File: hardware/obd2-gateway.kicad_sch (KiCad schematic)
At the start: 7 parts, among them J1 OBD-II 커넥터, U1 LM2596 (5.0V 조정), U2 SN65HVD230 (R2 제거!), U3 ESP32-S3 개발보드

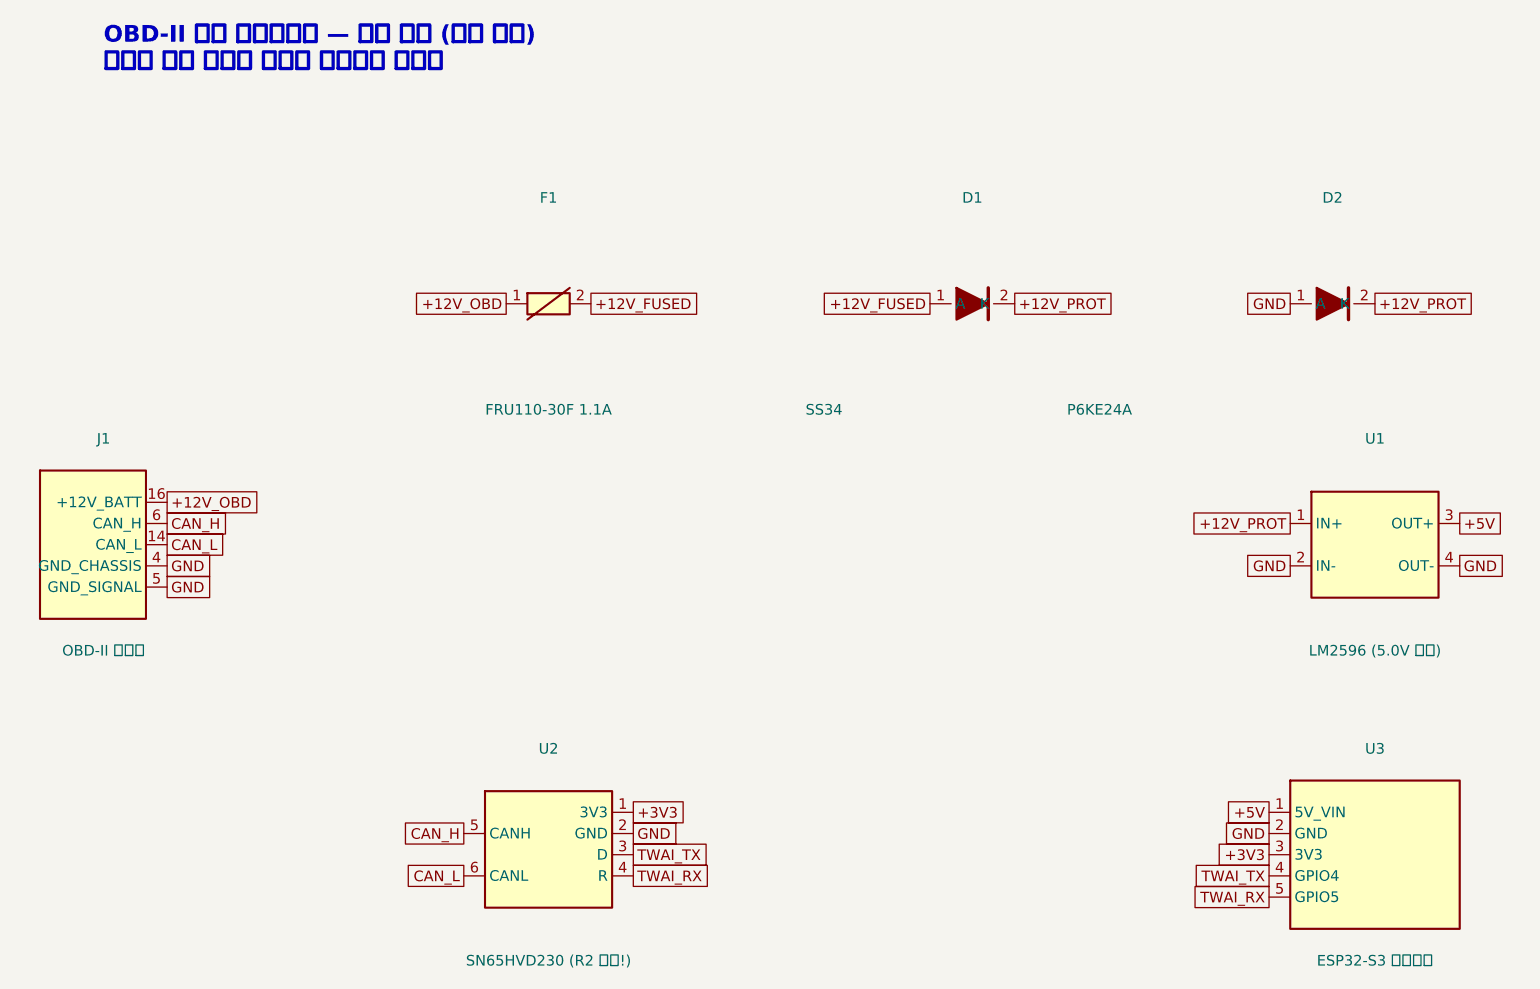
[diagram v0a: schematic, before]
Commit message: hardware: 회로도를 배선(wire) 방식으로 재작성 (Rev B, 초보자 가독성)
Co-Authored-By: Claude Fable 5 <noreply@anthropic.com>
Claude-Session: https://claude.ai/code/session_015Lj2iN8K2AKiUuQKmtXaeP
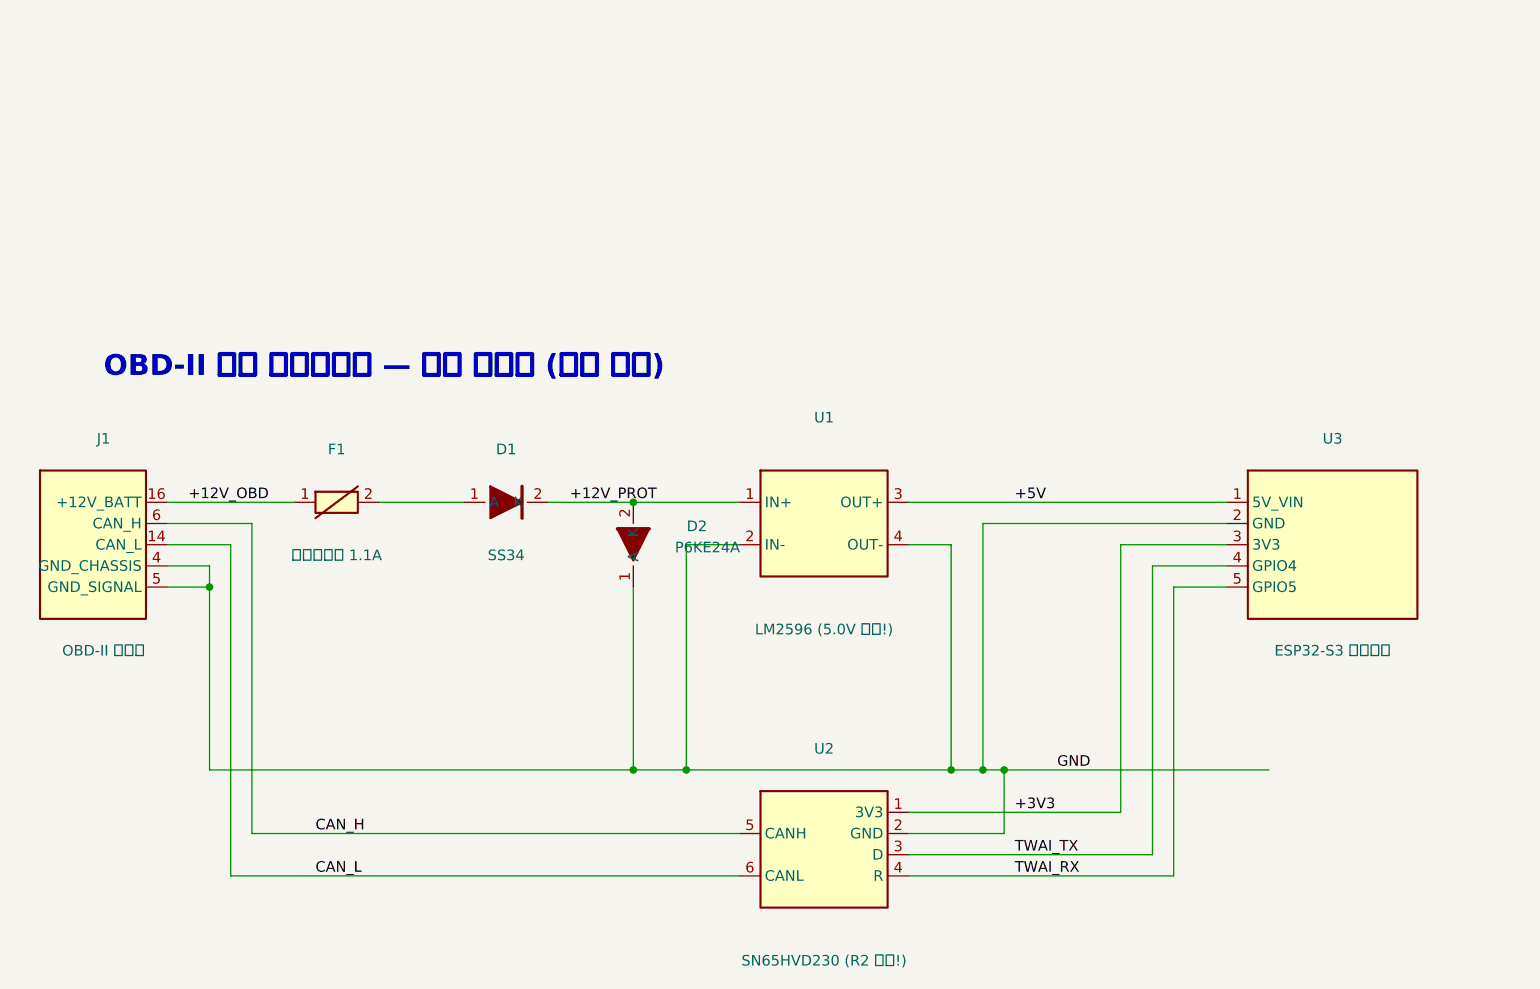
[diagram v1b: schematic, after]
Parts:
- removed D2: P6KE24A, symbol OBD2DIY:D_TVS_UNI
- added D2: P6KE24A, symbol OBD2DIY:D_TVS_V
- F1: value FRU110-30F 1.1A -> 폴리스위치 1.1A
- U1: value LM2596 (5.0V 조정) -> LM2596 (5.0V 조정!)
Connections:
- net +12V_PROT: now also D2.2 (K)
- net GND: now also D2.1 (A)
- net +12V_FUSED: no longer names the net of D1.1 (A), F1.2
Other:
- note added: "OBD-II 진단 게이트웨이 — 벤치 회로도 (배선 방식)"
- note removed: "OBD-II 진단 게이트웨이 — 벤치 회로 (모듈 단위) 연결은 같은 이름의 글로벌 라벨끼리 이어짐"
- title: OBD-II 진단 게이트웨이 — 벤치 회로도 -> OBD-II Diagnostic Gateway - Bench Wiring
